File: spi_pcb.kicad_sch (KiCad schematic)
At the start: 12 parts, among them J1 GPIO, U1 LMZ23605TZ

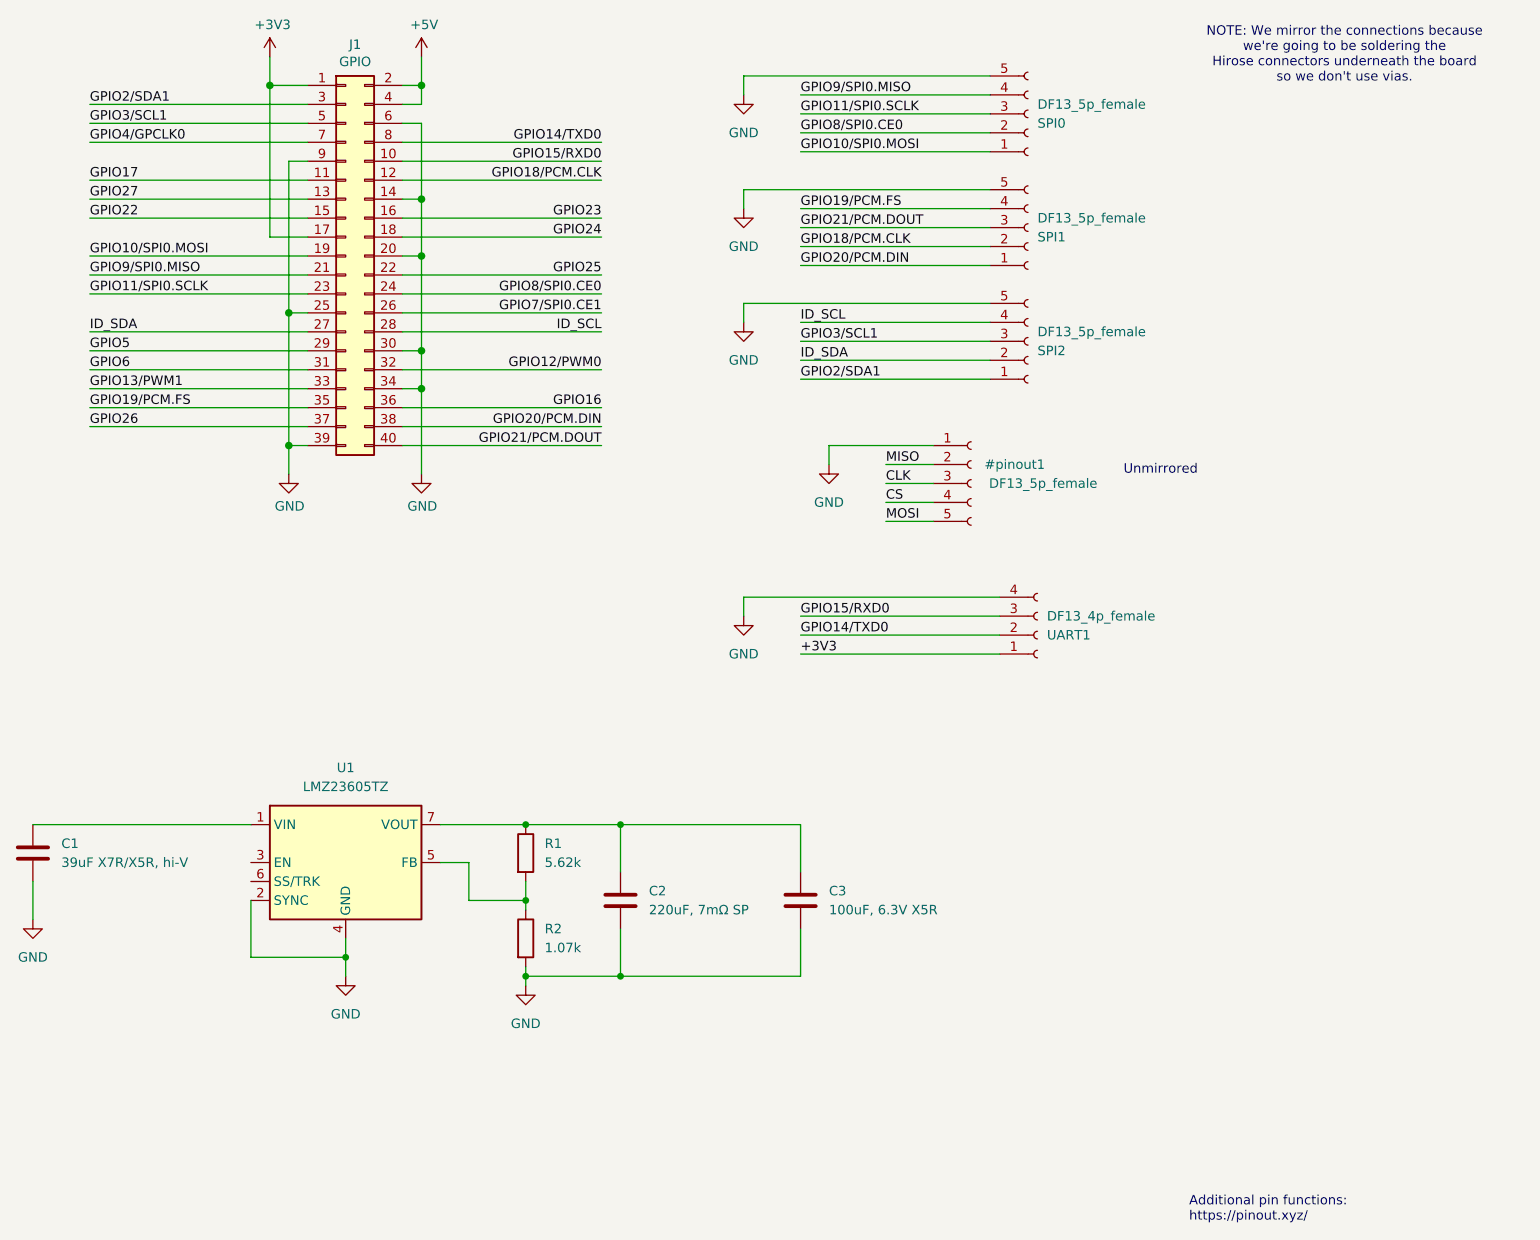
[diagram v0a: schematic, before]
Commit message: Sent connectors to back plane
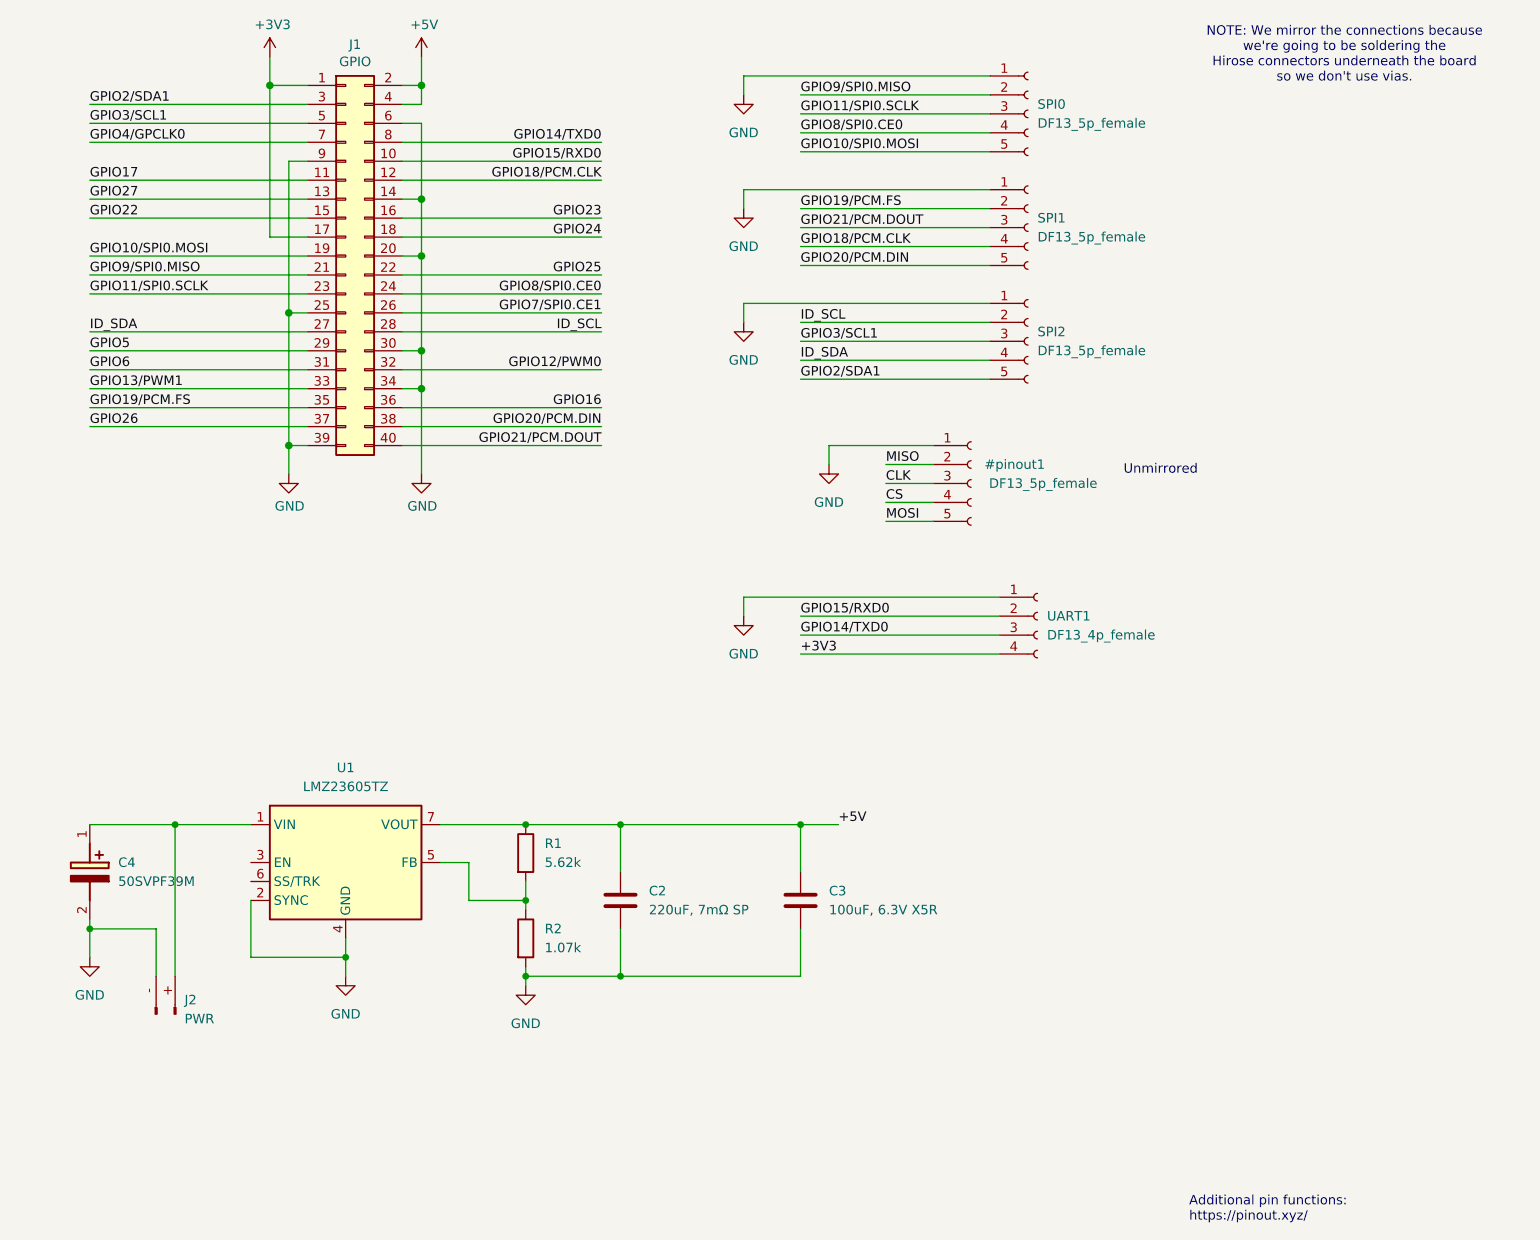
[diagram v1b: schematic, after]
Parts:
- removed C1: 39uF X7R/X5R, hi-V, symbol Device:C
- added C4: 50SVPF39M, 16SVPT560M, symbol SamacSys_Parts:50SVPF39M
- added J2: PWR, Connector_AMASS:AMASS_XT30PW-M_1x02_P2.50mm_Horizontal, symbol Connector:Conn_01x02_Pin
- R1: footprint (none) -> Capacitor_SMD:C_0603_1608Metric
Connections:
- net +3V3: now also UART1.4 (Pin_4); no longer UART1.1 (Pin_1)
- net +5V: now also C2.1, C3.1, R1.1, U1.7 (VOUT)
- net GND: now also SPI0.1 (Pin_1), SPI1.1 (Pin_1), SPI2.1 (Pin_1), UART1.1 (Pin_1), C4.2 (-), J2.- (Pin_1); no longer SPI0.5 (Pin_5), SPI1.5 (Pin_5), SPI2.5 (Pin_5), UART1.4 (Pin_4)
- net GPIO10/SPI0.MOSI: now also SPI0.5 (Pin_5); no longer SPI0.1 (Pin_1)
- net GPIO14/TXD0: now also UART1.3 (Pin_3); no longer UART1.2 (Pin_2)
- net GPIO15/RXD0: now also UART1.2 (Pin_2); no longer UART1.3 (Pin_3)
- net GPIO18/PCM.CLK: now also SPI1.4 (Pin_4); no longer SPI1.2 (Pin_2)
- net GPIO19/PCM.FS: now also SPI1.2 (Pin_2); no longer SPI1.4 (Pin_4)
- net GPIO20/PCM.DIN: now also SPI1.5 (Pin_5); no longer SPI1.1 (Pin_1)
- net GPIO2/SDA1: now also SPI2.5 (Pin_5); no longer SPI2.1 (Pin_1)
- net GPIO8/SPI0.CE0: now also SPI0.4 (Pin_4); no longer SPI0.2 (Pin_2)
- net GPIO9/SPI0.MISO: now also SPI0.2 (Pin_2); no longer SPI0.4 (Pin_4)
- net ID_SCL: now also SPI2.2 (Pin_2); no longer SPI2.4 (Pin_4)
- net ID_SDA: now also SPI2.4 (Pin_4); no longer SPI2.2 (Pin_2)
- net at U1.1 (VIN): now also C4.1 (+), J2.+ (Pin_2)

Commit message: V0
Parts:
- removed C2: 220uF, 7mΩ SP, symbol Device:C
- removed C3: 100uF, 6.3V X5R, symbol Device:C
- added C1: EEF-CX0J221R, EEFCX0J101R, symbol SamacSys_Parts:EEF-CX0J221R
- added C2: C3216X5R0J107M160AB, CAPC3216X180N, symbol SamacSys_Parts:C3216X5R0J107M160AB
- R1: footprint Capacitor_SMD:C_0603_1608Metric -> Resistor_SMD:R_0603_1608Metric
- R2: value 1.07k -> 1.05k; footprint (none) -> Resistor_SMD:R_0603_1608Metric
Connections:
- net +3V3: no longer J1.17 (Pin_17)
- net +5V: now also C1.1 (+), C2.1
- net GND: now also C1.2 (-), C2.2

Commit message: Correct schematic annotations
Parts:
- R1: value 5.62k -> 5.6k
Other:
- note added: "Vout = 0.796 * (1 + 5.6/1.05) = 5.04V"
- note removed: "NOTE: We mirror the connections because we're going to be soldering the Hirose connectors underneath the board so we don't use vias."
- note removed: "Unmirrored"
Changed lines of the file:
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@@
 		(date "15 nov 2012")
 	)
-	(text "Unmirrored\n"
-		(exclude_from_sim no)
-		(at 175.26 79.502 0)
-		(effects
-			(font
-				(size 1.27 1.27)
-			)
-		)
-	)
 	(text "Additional pin functions:\nhttps://pinout.xyz/"
 		(exclude_from_sim no)
@@
 		)
 	)
-	(text "NOTE: We mirror the connections because\nwe're going to be soldering the\nHirose connectors underneath the board\nso we don't use vias.\n"
+	(text "Vout = 0.796 * (1 + 5.6/1.05) = 5.04V"
 		(exclude_from_sim no)
-		(at 199.898 23.876 0)
+		(at 99.06 158.242 0)
 		(effects
 			(font
@@
 			)
 		)
-		(property "Value" "5.62k"
+		(property "Value" "5.6k"
 			(at 92.71 132.0799 0)
 			(effects

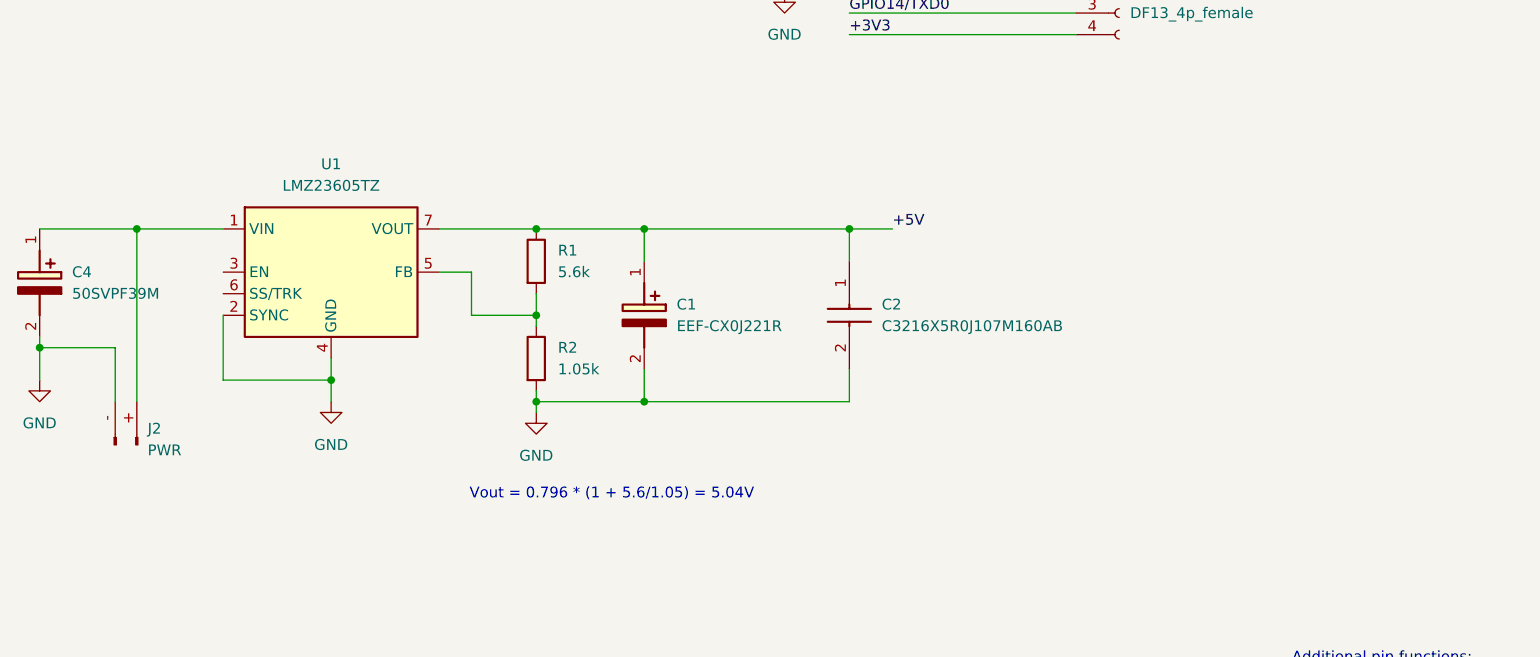
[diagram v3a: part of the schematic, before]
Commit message: Added VCC ceramic filter caps
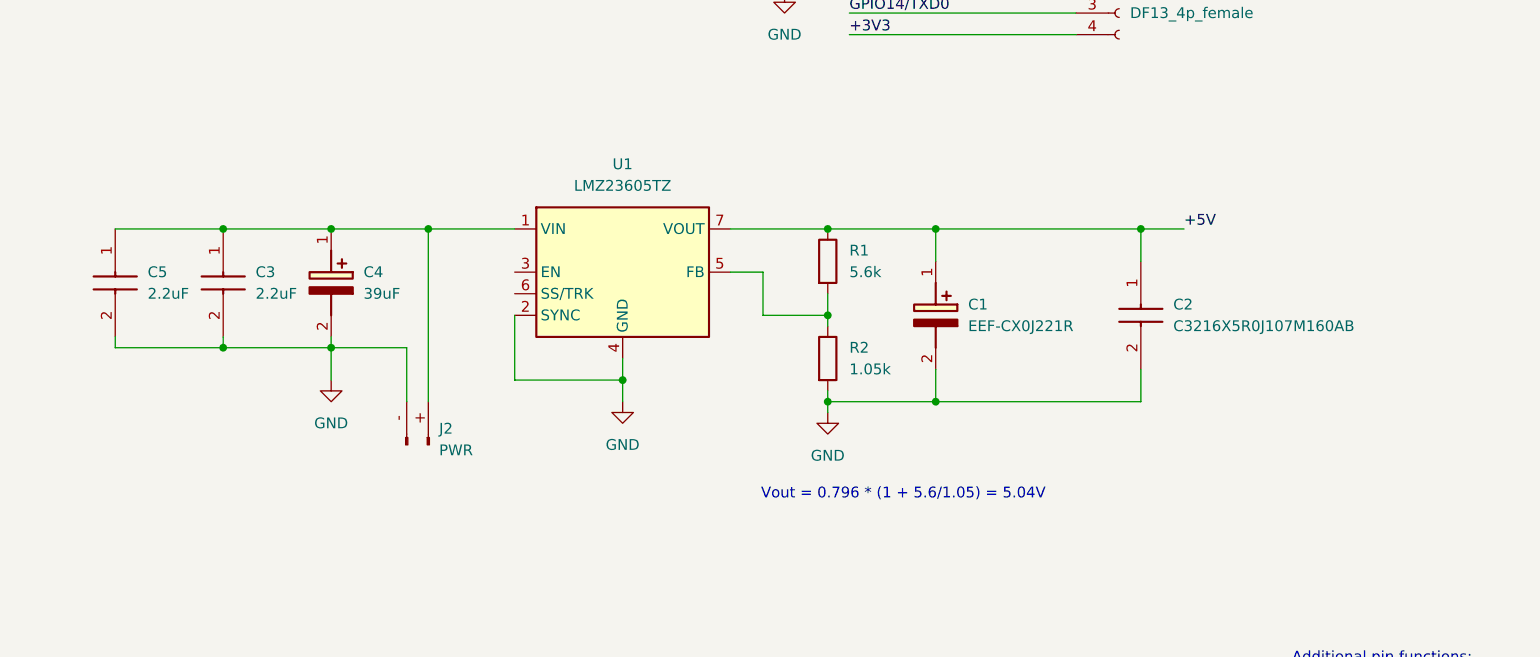
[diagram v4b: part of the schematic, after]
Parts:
- added C3, C5: 2.2uF, CAPC1608X90N, symbol SamacSys_Parts:GRT188R61H225KE13D
- C4: value 50SVPF39M -> 39uF
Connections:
- net GND: now also C3.2, C5.2
- net at C4.1 (+), J2.+ (Pin_2), U1.1 (VIN): now also C3.1, C5.1
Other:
- moved on the sheet: C1, C2, C4, J2, R1, R2, U1
